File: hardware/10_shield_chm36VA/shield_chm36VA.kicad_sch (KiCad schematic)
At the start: 28 parts, among them J1 Conn_01x04_Female, J10 Conn_01x10_Male, J11 Conn_01x10_Male, J12 Conn_01x06_Female, J13 Conn_01x09_Male, J14 Conn_01x02_Male, J15 Conn_01x06_Female, J16 Conn_01x06_Male, J17 Conn_01x06_Female, J18 Conn_01x06_Female, J19 Conn_01x09_Male, J2 Conn_01x06_Female, J20 Conn_01x02_Male, J21 Conn_01x06_Female, J22 Conn_01x10_Male, J23 Conn_01x06_Female, J24 Conn_01x02_Male, J25 Conn_01x10_Male, J26 Conn_01x10_Male, J27 Conn_02x05_Odd_Even, J28 Conn_02x05_Odd_Even, J3 Conn_01x06_Male, J4 Conn_01x04_Male, J5 Conn_01x10_Male, J6 Conn_01x04_Female, J7 Conn_01x04_Male, J8 Conn_01x06_Female, J9 Conn_01x06_Male

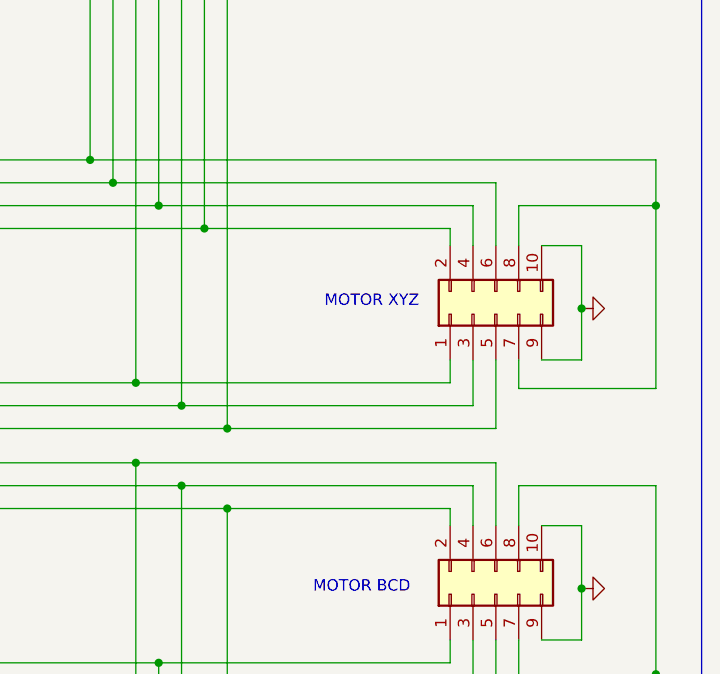
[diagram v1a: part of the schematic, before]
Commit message: Fixes in movement calculation. homing procedure fixed
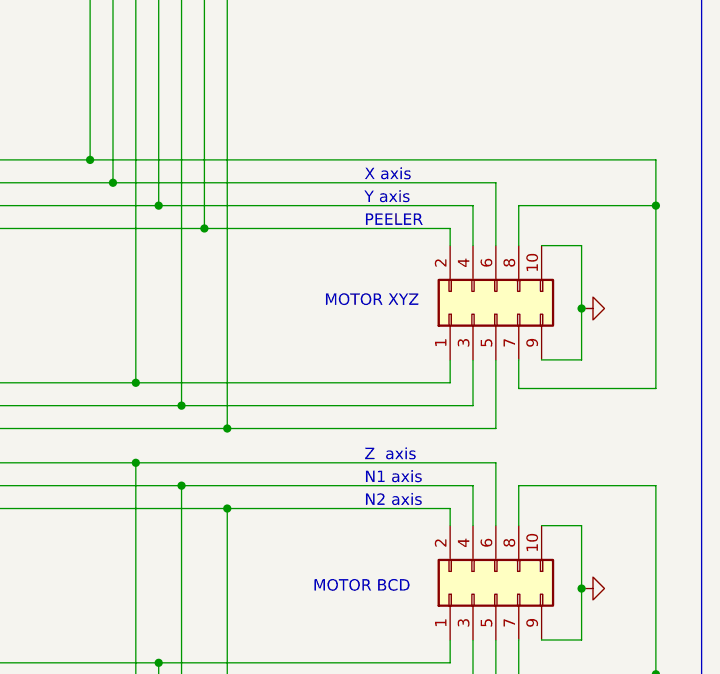
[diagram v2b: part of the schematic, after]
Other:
- note added: "N1 axis"
- note added: "N2 axis"
- note added: "PEELER"
- note added: "X axis"
- note added: "Y axis"
- note added: "Z axis"
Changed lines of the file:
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@@
     (stroke (width 0) (type default) (color 0 0 0 0))
+  )
+  (text "Z  axis" (at 354.33 157.48 0)
+    (effects (font (size 1.27 1.27)) (justify left bottom))
   )
   (text "brown" (at 252.73 62.23 90)
@@
     (effects (font (size 1.27 1.27)) (justify left bottom))
   )
+  (text "Y axis" (at 354.33 128.905 0)
+    (effects (font (size 1.27 1.27)) (justify left bottom))
+  )
   (text "white/pink" (at 174.625 64.135 90)
     (effects (font (size 1.27 1.27)) (justify left bottom))
   )
   (text "green" (at 155.829 60.833 90)
+    (effects (font (size 1.27 1.27)) (justify left bottom))
+  )
+  (text "N2 axis" (at 354.33 162.56 0)
     (effects (font (size 1.27 1.27)) (justify left bottom))
   )
@@
     (effects (font (size 1.27 1.27)) (justify left bottom))
   )
+  (text "X axis" (at 354.33 126.365 0)
+    (effects (font (size 1.27 1.27)) (justify left bottom))
+  )
   (text "grey" (at 247.65 62.23 90)
     (effects (font (size 1.27 1.27)) (justify left bottom))
   )
   (text "white/brown" (at 141.605 60.96 90)
+    (effects (font (size 1.27 1.27)) (justify left bottom))
+  )
+  (text "N1 axis" (at 354.33 160.02 0)
     (effects (font (size 1.27 1.27)) (justify left bottom))
   )
@@
     (effects (font (size 1.27 1.27)) (justify left bottom))
   )
+  (text "PEELER" (at 354.33 131.445 0)
+    (effects (font (size 1.27 1.27)) (justify left bottom))
+  )
